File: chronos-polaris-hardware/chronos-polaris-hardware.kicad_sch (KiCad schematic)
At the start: 25 parts, among them J1 Conn_01x03_Pin, J2 Conn_01x03_Pin, J3 Conn_01x03_Pin, J4 Conn_01x03_Pin, J5 Conn_01x03_Pin, J6 Conn_01x04, J7 Conn_01x04, J8 Conn_01x02, P1 WJ124-3_81-6P, U10 MSK12C02-HB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

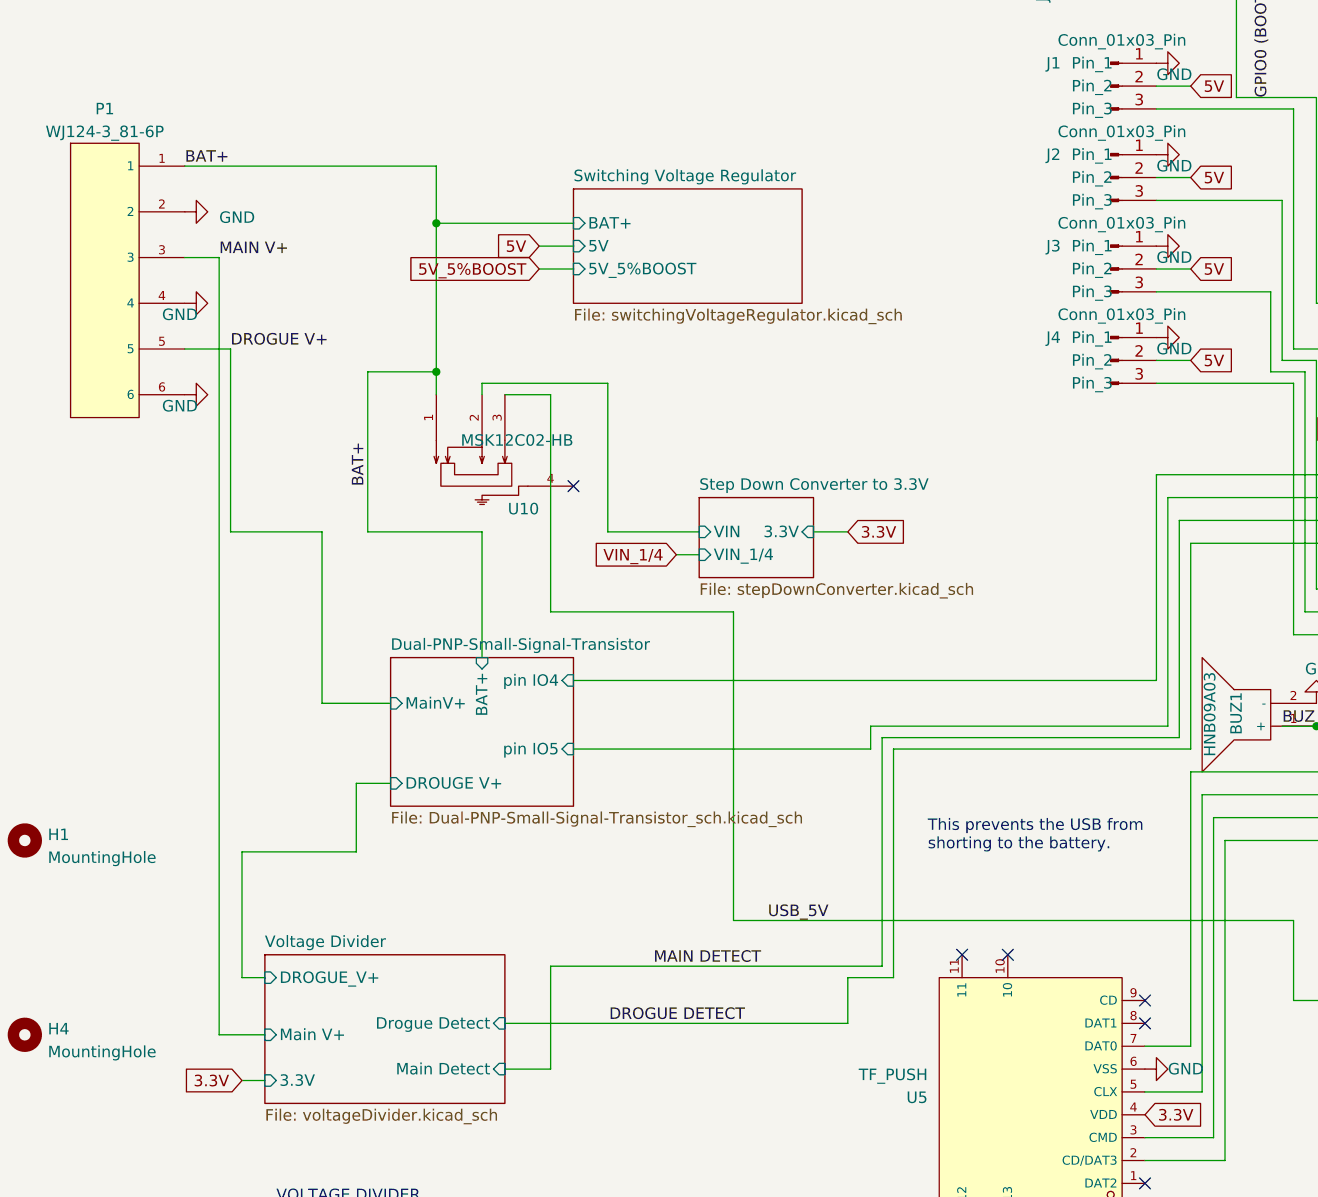
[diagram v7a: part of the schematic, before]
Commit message: E-match lowside switch
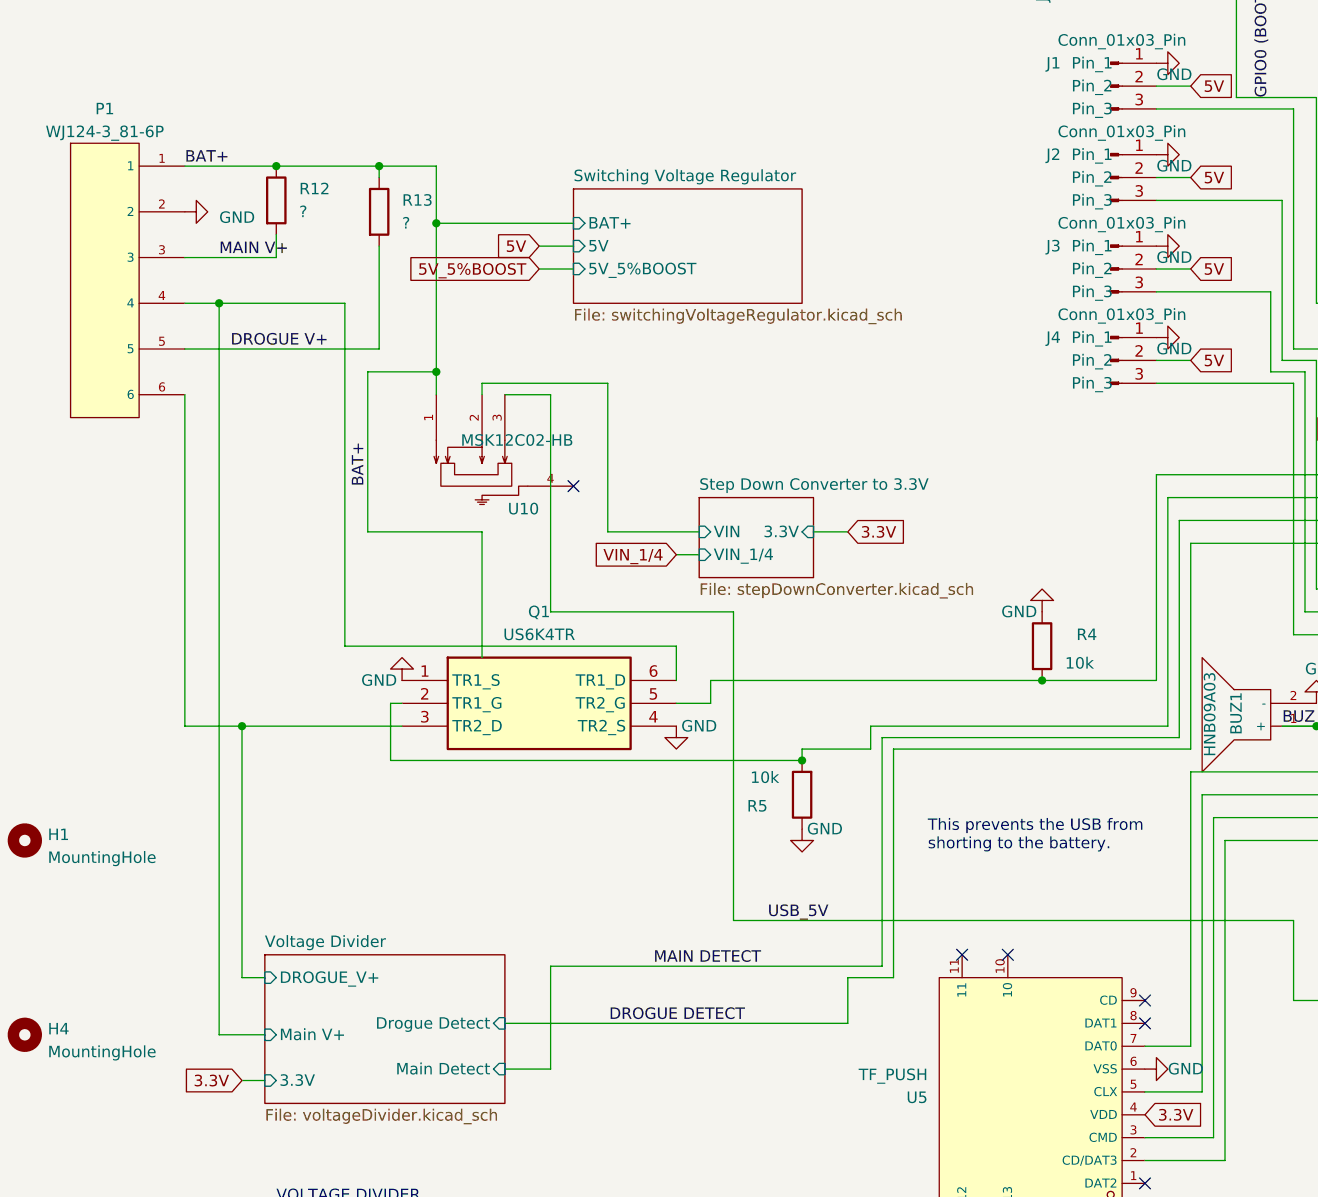
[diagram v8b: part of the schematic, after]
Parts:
- added Q1: US6K4TR, US6K4TR, symbol US6K4TR:US6K4TR
- added R12, R13: ?, Resistor_SMD:R_0603_1608Metric, symbol Device:R
- added R4, R5: 10k, Resistor_SMD:R_0603_1608Metric, symbol Device:R
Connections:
- net BAT+: now also R12.1, R13.1
- net DROGUE V+: now also R13.2
- net GND: now also Q1.1 (TR1_S), Q1.4 (TR2_S), R4.1, R5.1; no longer P1.4, P1.6
- net MAIN V+: now also R12.2
- net Dual-PNP-Small-Signal-Transistor/pin IO4: no longer names the net of U2.4 (IO4)
- net Dual-PNP-Small-Signal-Transistor/pin IO4: now also Q1.5 (TR2_G), R4.2
- net Dual-PNP-Small-Signal-Transistor/pin IO5: no longer names the net of U2.5 (IO5)
- net Dual-PNP-Small-Signal-Transistor/pin IO5: now also Q1.2 (TR1_G), R5.2
- new net Voltage Divider/DROGUE_V+: P1.6, Q1.3 (TR2_D)
- new net Voltage Divider/Main V+: P1.4, Q1.6 (TR1_D)
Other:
- removed sheet Dual-PNP-Small-Signal-Transistor
